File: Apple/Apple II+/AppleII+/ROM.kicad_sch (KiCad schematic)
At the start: 8 parts

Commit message: Started off-grid clean-up, 1900 to go!
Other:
- moved on the sheet: F12, H1B, ROM-D0, ROM-D8, ROM-E0, ROM-E8, ROM-F0, ROM-F8

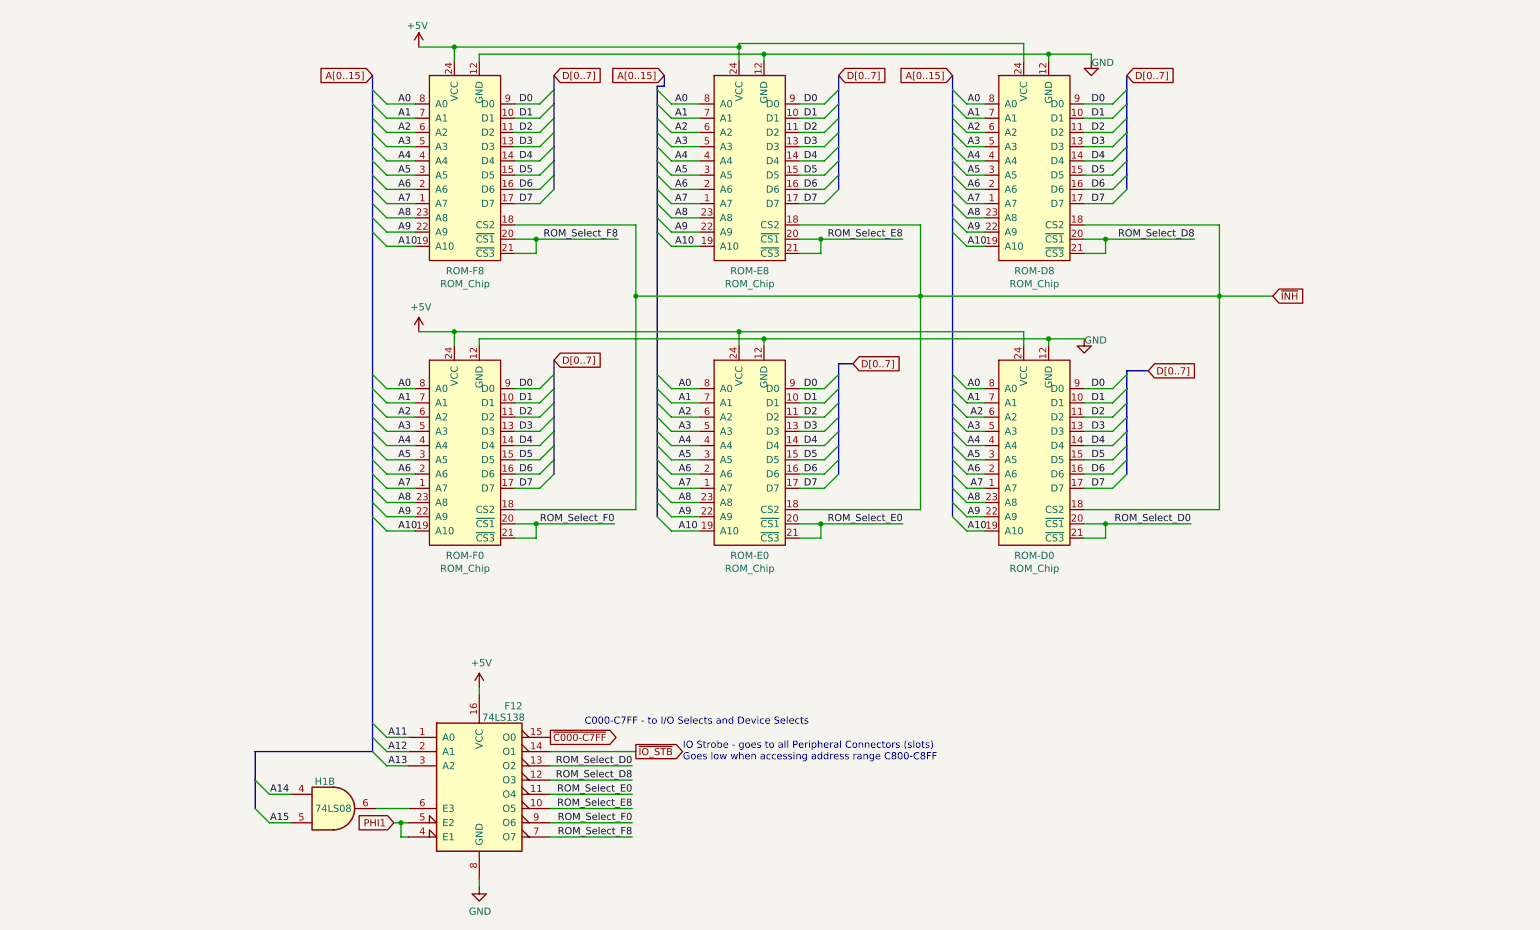
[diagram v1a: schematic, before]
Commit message: Started moving Global labels to Hierarchical and Local labels
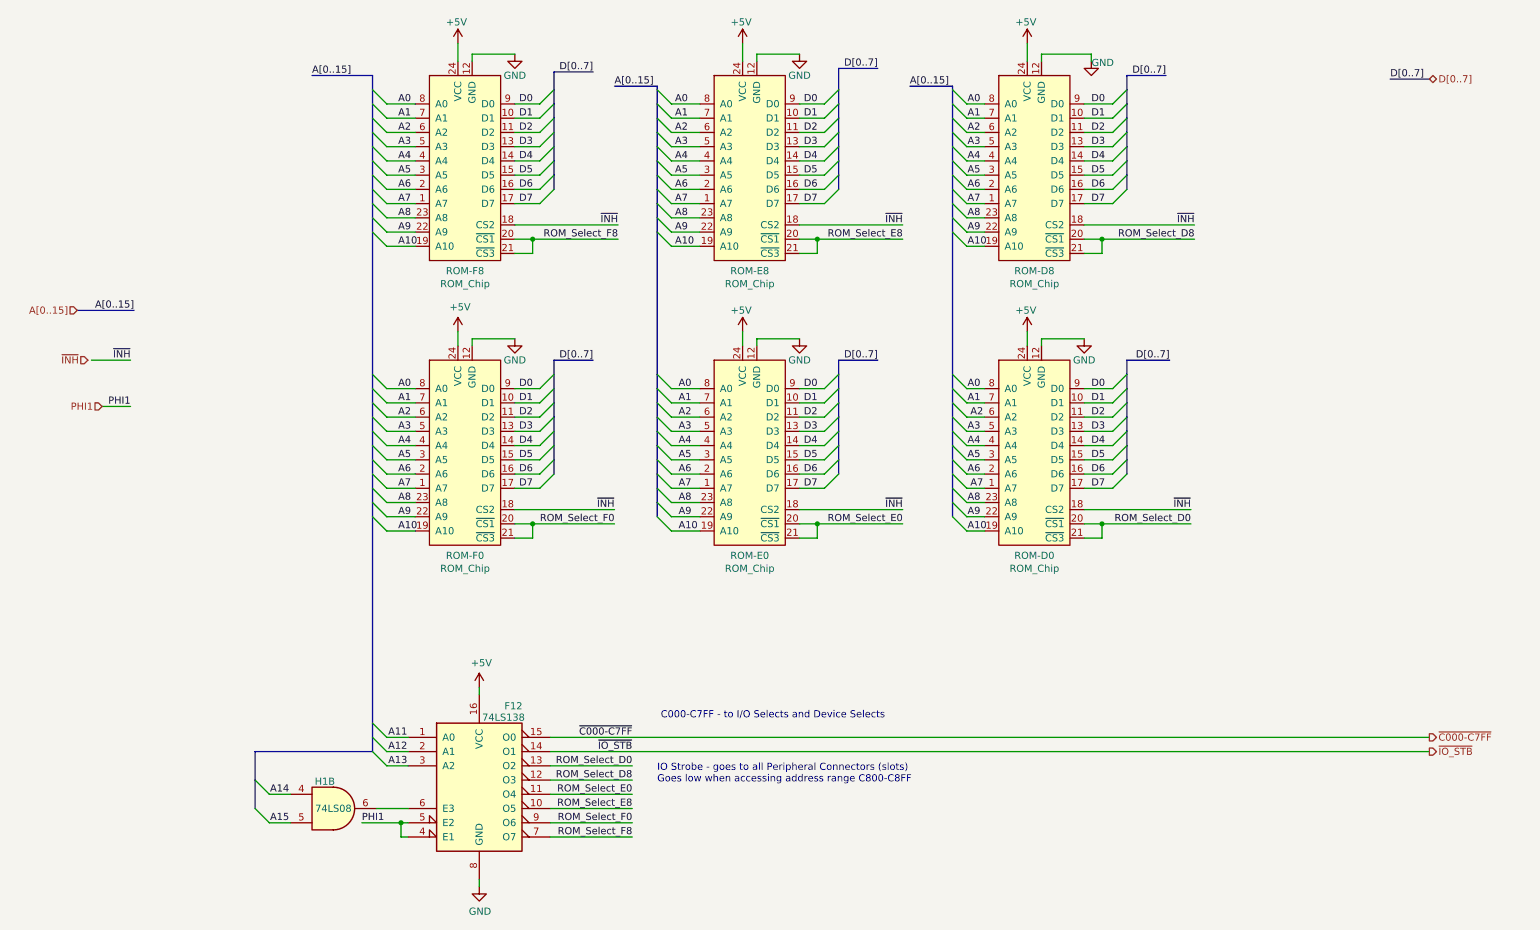
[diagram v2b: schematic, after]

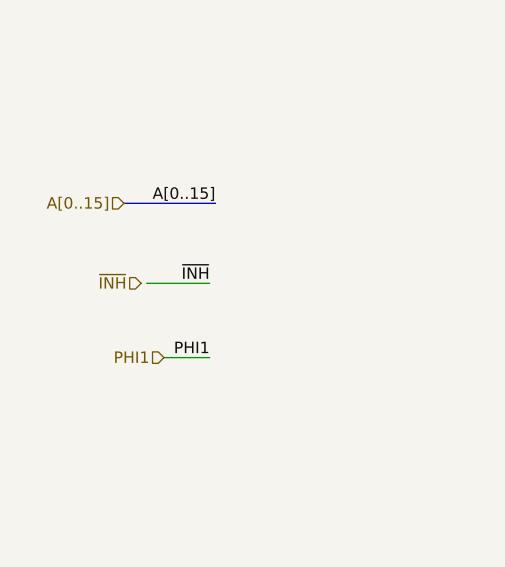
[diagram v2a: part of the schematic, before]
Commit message: Changed SOFT5-A2-8 and -11 to just SOFT5, based on Apple II Circuit Description Book
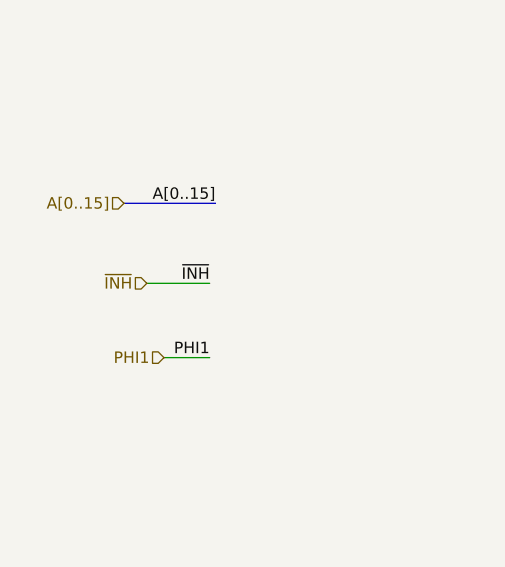
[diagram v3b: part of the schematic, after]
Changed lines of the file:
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@@
     (effects (font (size 1.27 1.27)) (justify right))
   )
-  (hierarchical_label "~{INH}" (shape input) (at 26.035 86.36 180) (fields_autoplaced)
+  (hierarchical_label "~{INH}" (shape input) (at 26.67 86.36 180) (fields_autoplaced)
     (effects (font (size 1.27 1.27)) (justify right))
   )

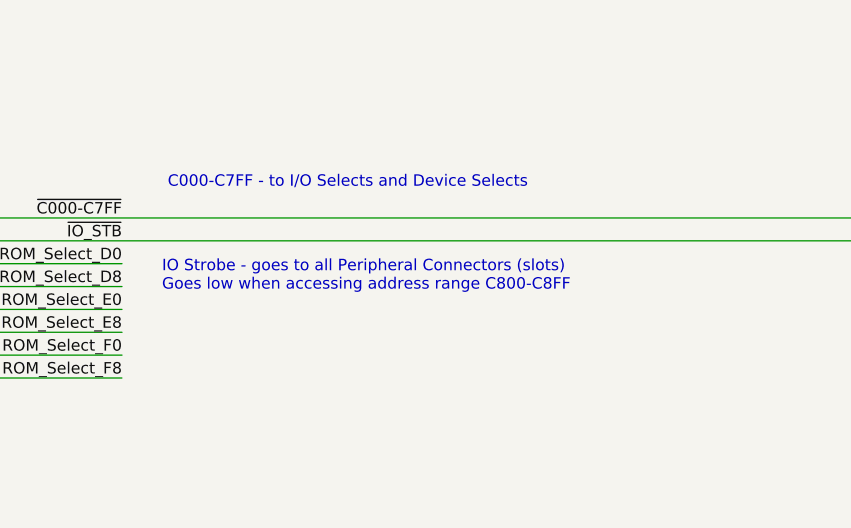
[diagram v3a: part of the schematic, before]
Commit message: fixed #125, F12 had the wrong address range listed and re-generated PDF
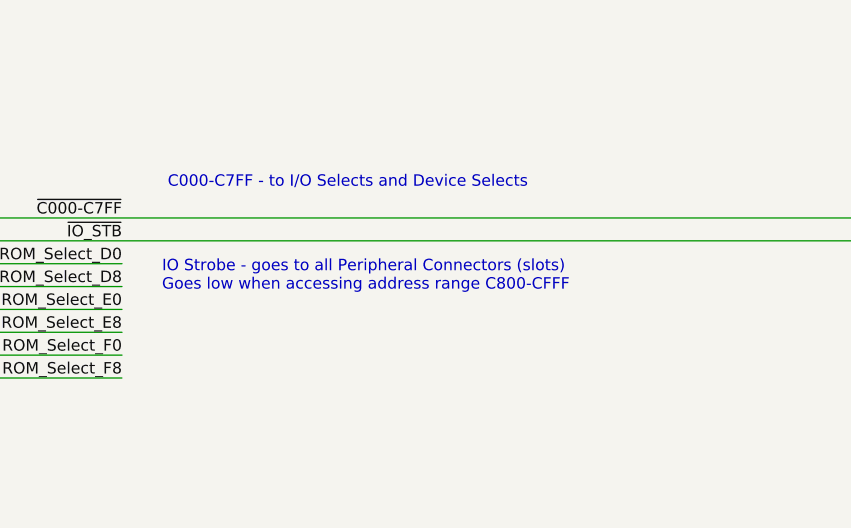
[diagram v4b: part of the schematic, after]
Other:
- note added: "IO Strobe - goes to all Peripheral Connectors (slots) Goes low when accessing address range C800-CFFF"
- note removed: "IO Strobe - goes to all Peripheral Connectors (slots) Goes low when accessing address range C800-C8FF"
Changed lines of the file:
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@@
     (stroke (width 0) (type default))
   )
-  (text "IO Strobe - goes to all Peripheral Connectors (slots)\nGoes low when accessing address range C800-C8FF"
+  (text "IO Strobe - goes to all Peripheral Connectors (slots)\nGoes low when accessing address range C800-CFFF"
     (at 127.635 161.925 0)
     (effects (font (size 1.27 1.27)) (justify left bottom))
